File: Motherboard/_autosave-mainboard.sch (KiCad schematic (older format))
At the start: 48 parts, among them IC1 BMX160, J1 Conn_01x01, J2 10118194-0001LF, J28 Conn_01x01, J29 Conn_01x01, J3 Micro_SD_Card, J30 Conn_01x01, J4 xf2m-2415-1a, J5 XF2M-1015-1A, SW1 KMR231NG LFS, U1 RFM95W-915S2, U2 ATSAMD51G_TQFN48, U3 DRV8848, U4 TPS82740BSIPR, U5 DRV8848, U6 MAX708RESA-T, U8 RFM95W-915S2, X1 ANTENNA_U.FL, X2 ANTENNA_U.FL

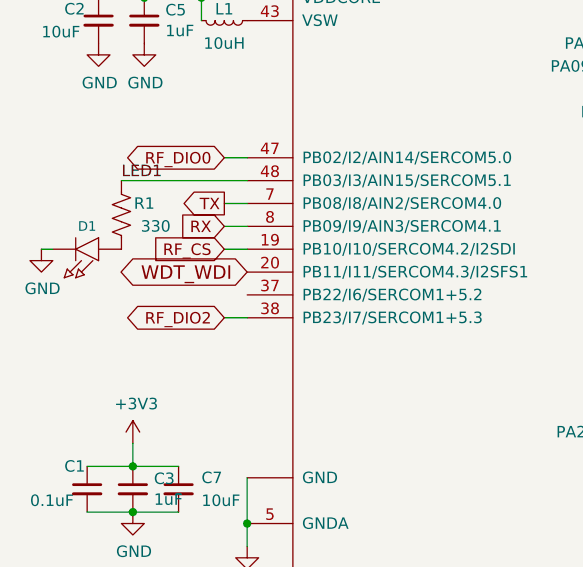
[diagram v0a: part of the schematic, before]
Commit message: added comm vias and traces to LoRa radio module on top layer
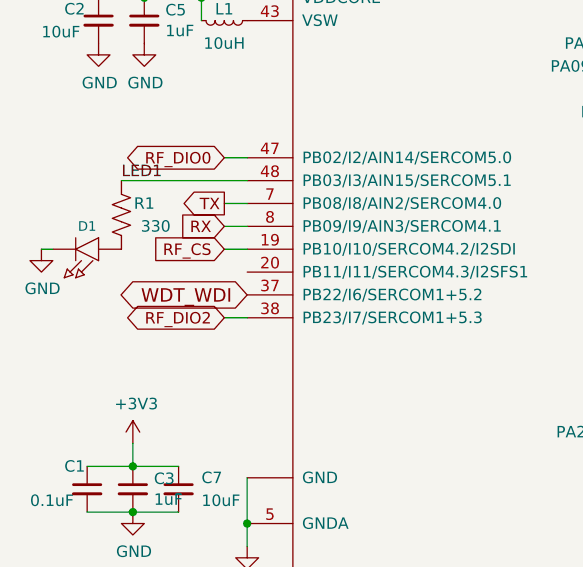
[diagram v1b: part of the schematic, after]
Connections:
- net WDT_WDI: now also U2.37 (PB22/I6/SERCOM1+5.2); no longer U2.20 (PB11/I11/SERCOM4.3/I2SFS1)
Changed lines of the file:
@@
 Text GLabel 5050 2950 0    50   Input ~ 0
 BATT_P
-Text GLabel 1450 5900 0    59   BiDi ~ 0
+Text GLabel 1450 6000 0    59   BiDi ~ 0
 WDT_WDI
 $EndSCHEMATC
